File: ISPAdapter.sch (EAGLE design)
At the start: 9 parts, among them J2 M02PTH, J3 M01PTH, J4 M01PTH, P1 AVX9258, U1 74LVC4066PW

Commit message: Pin order change
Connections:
- removed net AUX: J3.1, P1.5
- new net PB3: J3.1, P1.6
- net RESET: now also P1.5; no longer P1.6
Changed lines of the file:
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@@
 </segment>
 <segment>
-<pinref part="P1" gate="G$1" pin="6"/>
-<wire x1="104.14" y1="55.88" x2="104.14" y2="53.34" width="0.1524" layer="91"/>
-<label x="104.14" y="53.34" size="1.27" layer="95" rot="R270" xref="yes"/>
+<pinref part="P1" gate="G$1" pin="5"/>
+<wire x1="106.68" y1="55.88" x2="106.68" y2="53.34" width="0.1524" layer="91"/>
+<label x="106.68" y="53.34" size="1.27" layer="95" rot="R270" xref="yes"/>
 </segment>
 </net>
@@
 </segment>
 </net>
-<net name="AUX" class="0">
+<net name="PB3" class="0">
 <segment>
 <pinref part="J3" gate="G$1" pin="1"/>
@@
 </segment>
 <segment>
-<pinref part="P1" gate="G$1" pin="5"/>
-<wire x1="106.68" y1="55.88" x2="106.68" y2="53.34" width="0.1524" layer="91"/>
-<label x="106.68" y="53.34" size="1.27" layer="95" rot="R270" xref="yes"/>
+<pinref part="P1" gate="G$1" pin="6"/>
+<wire x1="104.14" y1="55.88" x2="104.14" y2="53.34" width="0.1524" layer="91"/>
+<label x="104.14" y="53.34" size="1.27" layer="95" rot="R270" xref="yes"/>
 </segment>
 </net>

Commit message: Tweaks
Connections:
- net PB3: now also P1.5; no longer P1.6
- net RESET: now also P1.6; no longer P1.5
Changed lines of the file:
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@@
 </segment>
 <segment>
-<pinref part="P1" gate="G$1" pin="5"/>
-<wire x1="106.68" y1="55.88" x2="106.68" y2="53.34" width="0.1524" layer="91"/>
-<label x="106.68" y="53.34" size="1.27" layer="95" rot="R270" xref="yes"/>
+<pinref part="P1" gate="G$1" pin="6"/>
+<wire x1="104.14" y1="55.88" x2="104.14" y2="53.34" width="0.1524" layer="91"/>
+<label x="104.14" y="53.34" size="1.27" layer="95" rot="R270" xref="yes"/>
 </segment>
 </net>
@@
 </segment>
 <segment>
-<pinref part="P1" gate="G$1" pin="6"/>
-<wire x1="104.14" y1="55.88" x2="104.14" y2="53.34" width="0.1524" layer="91"/>
-<label x="104.14" y="53.34" size="1.27" layer="95" rot="R270" xref="yes"/>
+<pinref part="P1" gate="G$1" pin="5"/>
+<wire x1="106.68" y1="55.88" x2="106.68" y2="53.34" width="0.1524" layer="91"/>
+<label x="106.68" y="53.34" size="1.27" layer="95" rot="R270" xref="yes"/>
 </segment>
 </net>

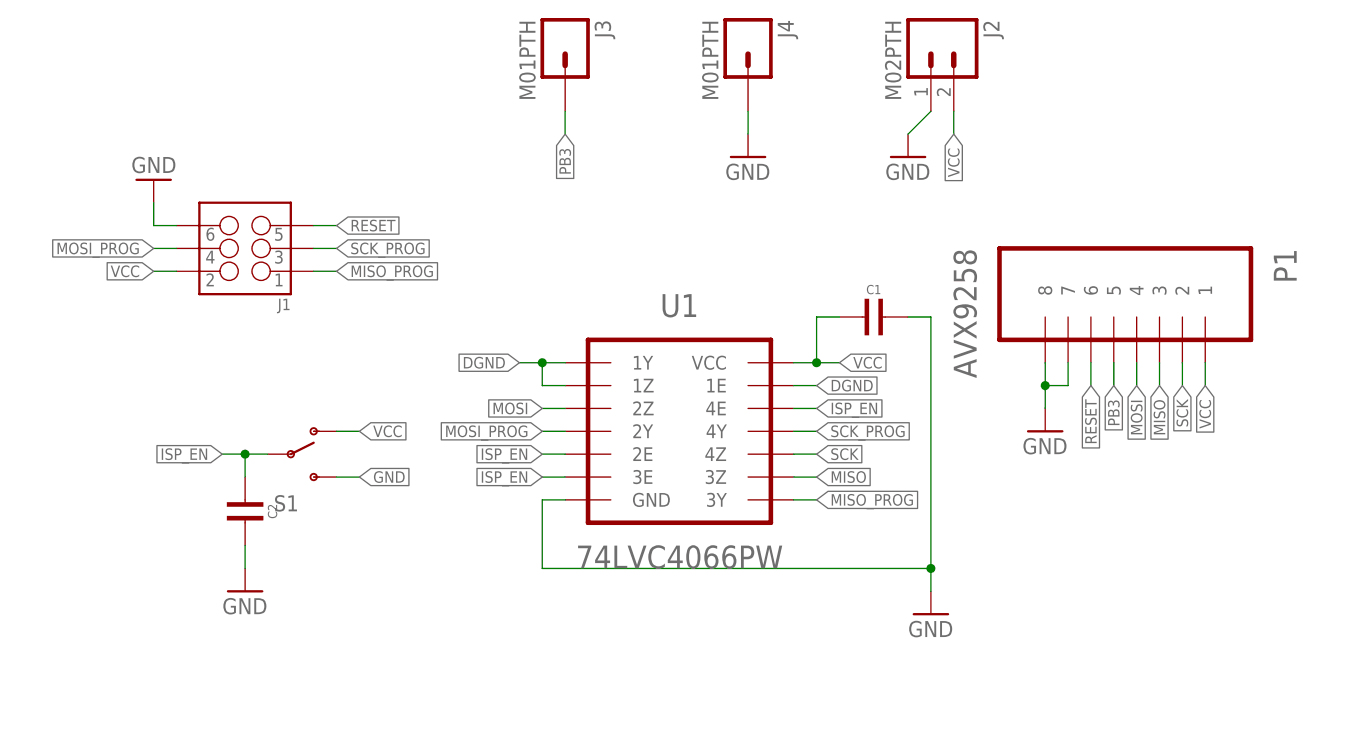
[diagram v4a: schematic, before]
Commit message: Debounce, grounding
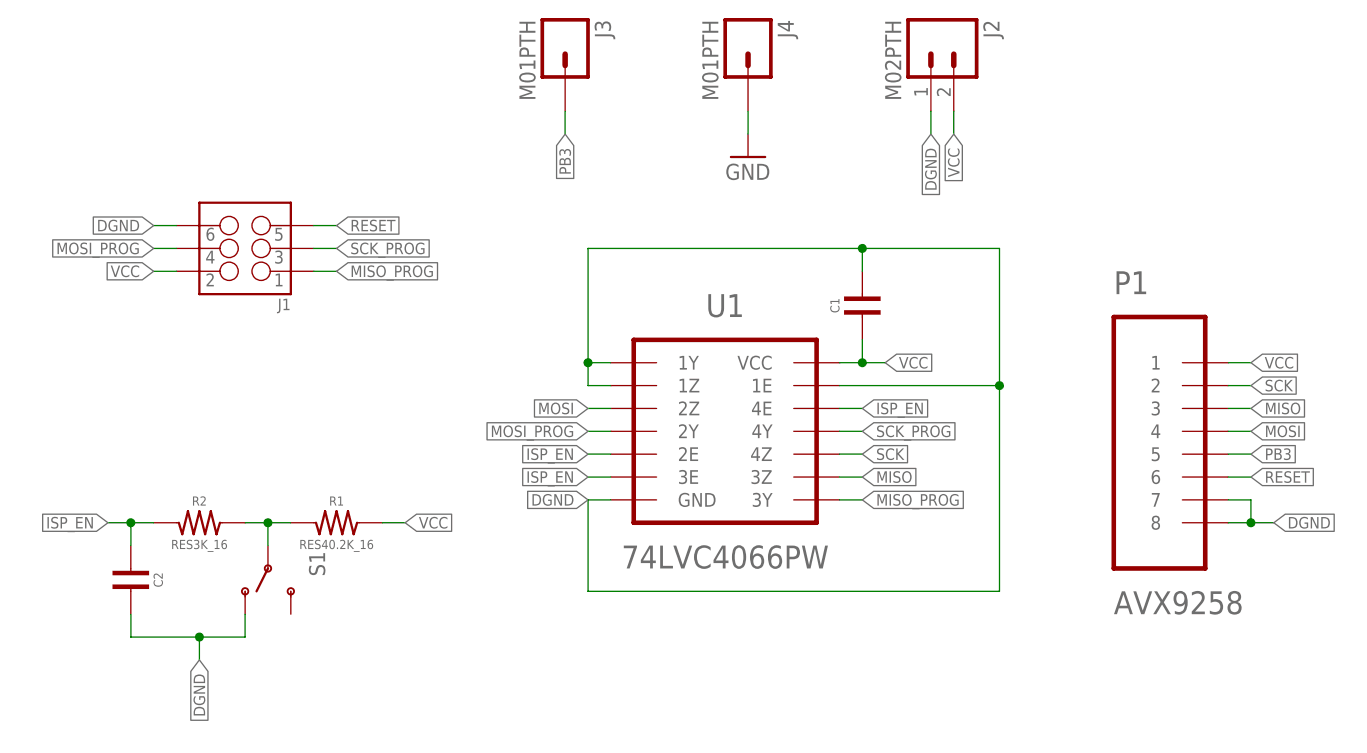
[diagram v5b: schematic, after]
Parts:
- added R1: RES40.2K_16, dubec:RES40.2K_16
- added R2: RES3K_16, dubec:RES3K_16
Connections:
- new net SWGND: R1.1, R2.2, S1.P
- net DGND: now also S1.O
- net GND: no longer S1.S
- net ISP_EN: now also R2.1; no longer S1.P
- net VCC: now also R1.2; no longer S1.O
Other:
- moved on the sheet: C1, C2, P1, S1, U1

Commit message: Tweaks
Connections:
- new net N$1: S1.S
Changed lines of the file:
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@@
+</segment>
+</net>
+<net name="N$1" class="0">
+<segment>
+<pinref part="S1" gate="1" pin="S"/>
+<wire x1="15.24" y1="27.94" x2="15.24" y2="25.4" width="0.1524" layer="91"/>
 </segment>
 </net>
